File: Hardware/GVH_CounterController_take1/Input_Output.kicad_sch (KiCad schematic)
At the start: 4 parts, among them J4 Molex Micro-Fit 5pos, U4 74AHCT2G125, U6 74AHCT2G125

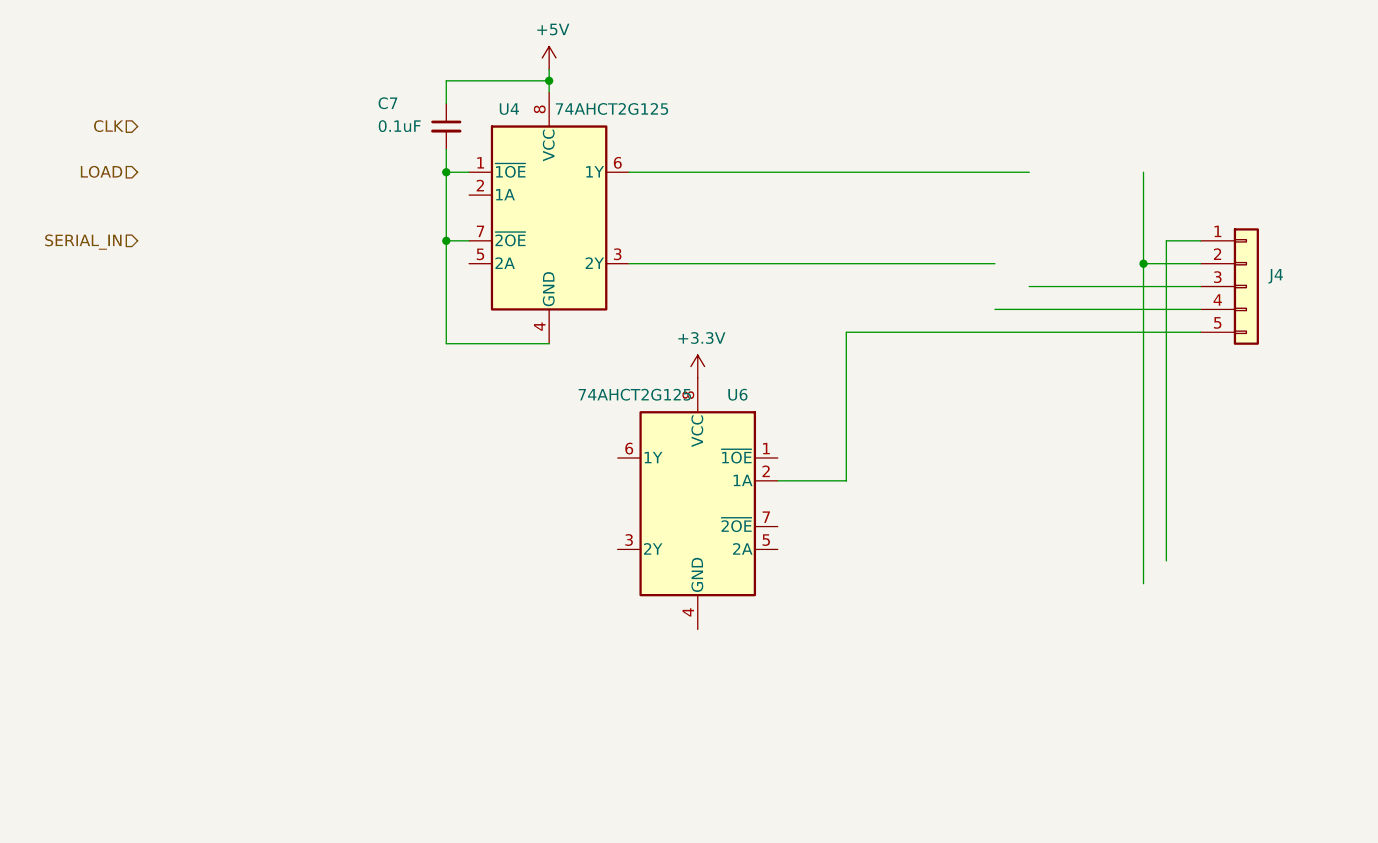
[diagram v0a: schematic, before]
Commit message: Counter Controller PCB - Added IO Level Shifter Sheet, Updated from Template
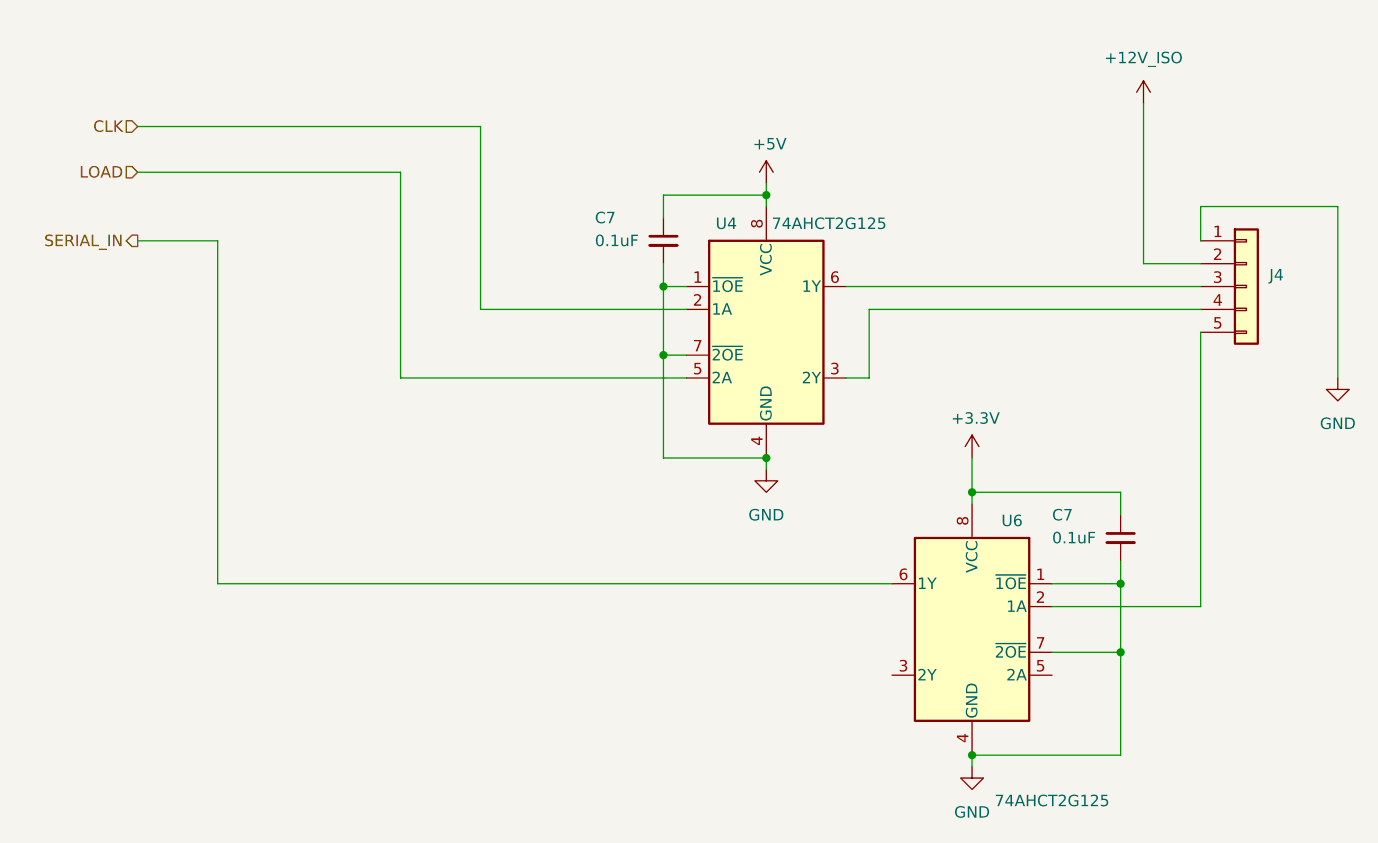
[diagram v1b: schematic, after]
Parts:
- added C7: 0.1uF, Capacitor_SMD:C_0402_1005Metric, symbol Device:C_Small
- C7: footprint Capacitor_SMD:C_0805_2012Metric -> Capacitor_SMD:C_0402_1005Metric
- J4: MPN (none) -> 0436500500; Mfg. P/N 0436500500 -> (none)
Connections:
- net +3.3V: now also C7.1
- net CLK: now also U4.2 (1A)
- net LOAD: now also U4.5 (2A)
- net SERIAL_IN: now also U6.6 (1Y)
- net GND: now reaches C7.2, U4.1 (~{1OE}), U4.4 (GND), U4.7 (~{2OE})
- net GND: now also J4.1 (Pin_1), U6.1 (~{1OE}), U6.4 (GND), U6.7 (~{2OE}), C7.2
- net at U4.3 (2Y): now also J4.4 (Pin_4)
- net at U4.6 (1Y): now also J4.3 (Pin_3)
- net +12V_ISO: now reaches J4.2 (Pin_2)
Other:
- moved on the sheet: C7, U4, U6
